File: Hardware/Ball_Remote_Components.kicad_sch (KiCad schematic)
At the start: 51 parts, among them J1 USB_B_Micro, J2 I2C_Gyro_Module, J3 SWD_Header, Q1 SI2333DS, U1 STM32WB35, U2 L3GD20, U3 MCP73831-2-OT, U4 LD3985M28R_SOT23, Y1 32MHz, Y2 32.768MHz

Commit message: Remote schematic and PCB clean up
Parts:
- added H1, H2: MountingHole, MountingHole:MountingHole_3.2mm_M3, symbol Mechanical:MountingHole
- added R2: 100k, Resistor_SMD:R_0603_1608Metric, symbol Device:R_Small
- added SW1: SW_SPDT, Custom_Footprints:SPDT_Slide_Switch, symbol Switch:SW_SPDT
- J1: renamed from J2; footprint Connector_PinSocket_2.54mm:PinSocket_1x06_P2.54mm_Vertical -> Connector_PinSocket_2.54mm:PinSocket_1x10_P2.54mm_Vertical; symbol Connector:Conn_01x06_Male -> Connector:Conn_01x10_Male
- renumbered C7 to C10, C18 to C11, C19 to C12, C14 to C13, C8 to C14, C9 to C15, C12 to C16, C13 to C17, C20 to C18, C21 to C19, C10 to C2, C22 to C20, C15 to C21, C16 to C22, C11 to C3, C17 to C4, C2 to C5, C3 to C6, C4 to C7, C5 to C8, C6 to C9, D2 to D1, D3 to D2, D1 to D3, J1 to J2, R3 to R1, R6 to R3, R2 to R4, R4 to R5, R5 to R6, R1 to R8, U3 to U1, U1 to U3
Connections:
- net +3V3 is gone; now on net +2V8: J3.1 (Pin_1)
- net GND: now also R2.1
- net USB_VIN: now also R2.2
- net BATT_+ renamed BATT_ON_OFF
- net BATT_ON_OFF: now also SW1.1 (A); no longer BT1.1 (+)
- new net BATT+: BT1.1 (+), SW1.2 (B)
- no-connect marks 16 -> 21
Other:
- note added: "Gyroscope and USB"
- note added: "LED/Buttons"
- note added: "MCU and RF"
- note added: "VCC will be 5V when connected to USB or 3.7-4.3V when battery powered NB R2 is pull-down for Q1"
- note removed: "Connectors/Buttons"
- note removed: "MCU"
- note removed: "VCC will be 5V when connected to USB or 3.7-4.3V when battery powered"
- moved on the sheet: AE1, C11, C12, C13, C18, C19, C2, C20, C21, C22, C3, C4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

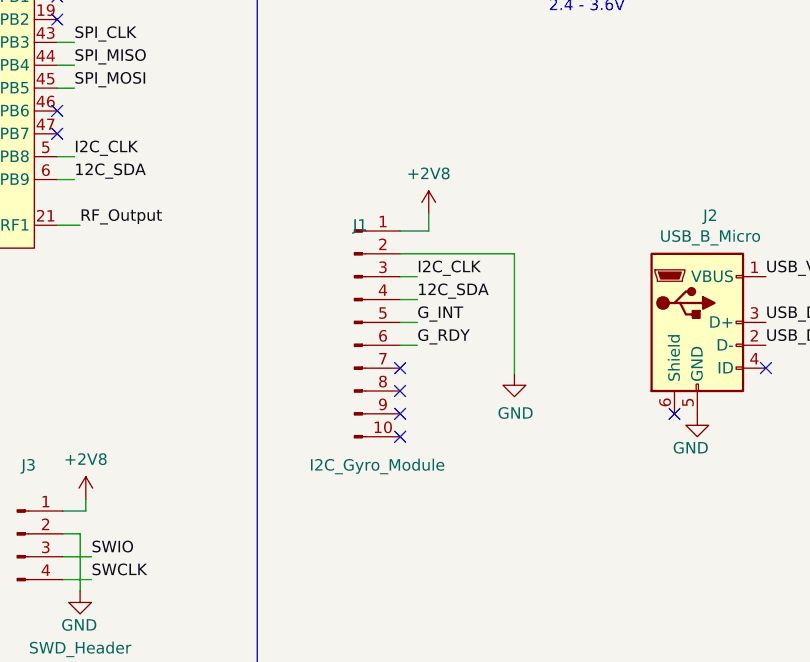
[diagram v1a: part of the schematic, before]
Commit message: More PCB clean-up
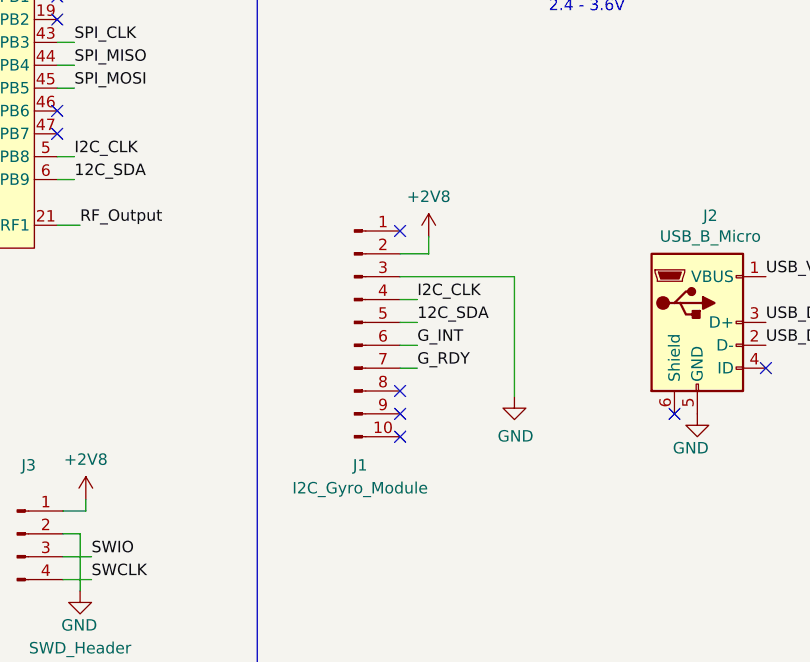
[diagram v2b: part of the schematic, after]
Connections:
- net +2V8: now also J1.2 (Pin_2); no longer J1.1 (Pin_1)
- net 12C_SDA: now also J1.5 (Pin_5); no longer J1.4 (Pin_4)
- net GND: now also J1.3 (Pin_3); no longer J1.2 (Pin_2)
- net G_INT: now also J1.6 (Pin_6); no longer J1.5 (Pin_5)
- net G_RDY: now also J1.7 (Pin_7); no longer J1.6 (Pin_6)
- net I2C_CLK: now also J1.4 (Pin_4); no longer J1.3 (Pin_3)
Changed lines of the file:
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@@
   (no_connect (at 86.995 77.47))
   (no_connect (at 86.995 92.71))
+  (no_connect (at 125.095 106.045))
   (no_connect (at 86.995 95.25))
   (no_connect (at 86.995 46.99))
@@
   (no_connect (at 56.515 95.25))
   (no_connect (at 125.095 126.365))
-  (no_connect (at 125.095 121.285))
   (wire (pts (xy 254.635 42.545) (xy 267.97 42.545))
     (stroke (width 0) (type default) (color 0 0 0 0))
@@
     (stroke (width 0) (type default) (color 0 0 0 0))
   )
-  (wire (pts (xy 125.095 106.045) (xy 128.27 106.045))
+  (wire (pts (xy 125.095 108.585) (xy 128.27 108.585))
     (stroke (width 0) (type default) (color 0 0 0 0))
   )
@@
     (stroke (width 0) (type default) (color 0 0 0 0))
   )
-  (wire (pts (xy 125.095 116.205) (xy 127 116.205))
-    (stroke (width 0) (type default) (color 0 0 0 0))
-  )
   (wire (pts (xy 125.095 118.745) (xy 127 118.745))
     (stroke (width 0) (type default) (color 0 0 0 0))
   )
+  (wire (pts (xy 125.095 121.285) (xy 127 121.285))
+    (stroke (width 0) (type default) (color 0 0 0 0))
+  )
   (wire (pts (xy 199.39 33.02) (xy 212.09 33.02))
     (stroke (width 0) (type default) (color 0 0 0 0))
@@
     (stroke (width 0) (type default) (color 0 0 0 0))
   )
-  (wire (pts (xy 137.795 108.585) (xy 137.795 121.92))
+  (wire (pts (xy 137.795 111.125) (xy 137.795 124.46))
     (stroke (width 0) (type default) (color 0 0 0 0))
   )
@@
     (stroke (width 0) (type default) (color 0 0 0 0))
   )
-  (wire (pts (xy 125.095 108.585) (xy 137.795 108.585))
+  (wire (pts (xy 125.095 111.125) (xy 137.795 111.125))
     (stroke (width 0) (type default) (color 0 0 0 0))
   )
@@
     (stroke (width 0) (type default) (color 0 0 0 0))
   )
-  (wire (pts (xy 128.27 106.045) (xy 128.27 104.14))
+  (wire (pts (xy 128.27 108.585) (xy 128.27 106.68))
     (stroke (width 0) (type default) (color 0 0 0 0))
   )
@@
     (stroke (width 0) (type default) (color 0 0 0 0))
   )
+  (wire (pts (xy 125.095 116.205) (xy 127 116.205))
+    (stroke (width 0) (type default) (color 0 0 0 0))
+  )
+  (wire (pts (xy 86.995 64.77) (xy 88.9 64.77))
+    (stroke (width 0) (type default) (color 0 0 0 0))
+  )
+  (wire (pts (xy 199.39 48.895) (xy 199.39 47.625))
+    (stroke (width 0) (type default) (color 0 0 0 0))
+  )
+  (wire (pts (xy 53.975 102.87) (xy 56.515 102.87))
+    (stroke (width 0) (type default) (color 0 0 0 0))
+  )
+  (wire (pts (xy 162.56 31.115) (xy 162.56 32.385))
+    (stroke (width 0) (type default) (color 0 0 0 0))
+  )
+  (wire (pts (xy 46.355 24.13) (xy 46.355 25.4))
+    (stroke (width 0) (type default) (color 0 0 0 0))
+  )
+  (wire (pts (xy 125.73 63.5) (xy 128.905 63.5))
+    (stroke (width 0) (type default) (color 0 0 0 0))
+  )
+  (wire (pts (xy 16.51 41.91) (xy 23.495 41.91))
+    (stroke (width 0) (type default) (color 0 0 0 0))
+  )
+  (wire (pts (xy 39.37 145.415) (xy 44.45 145.415))
+    (stroke (width 0) (type default) (color 0 0 0 0))
+  )
+  (wire (pts (xy 220.98 130.175) (xy 229.235 130.175))
+    (stroke (width 0) (type default) (color 0 0 0 0))
+  )
+  (wire (pts (xy 128.905 66.04) (xy 125.73 66.04))
+    (stroke (width 0) (type default) (color 0 0 0 0))
+  )
+  (wire (pts (xy 222.25 47.625) (xy 224.155 47.625))
+    (stroke (width 0) (type default) (color 0 0 0 0))
+  )
   (wire (pts (xy 125.095 113.665) (xy 127 113.665))
-    (stroke (width 0) (type default) (color 0 0 0 0))
-  )
-  (wire (pts (xy 86.995 64.77) (xy 88.9 64.77))
-    (stroke (width 0) (type default) (color 0 0 0 0))
-  )
-  (wire (pts (xy 199.39 48.895) (xy 199.39 47.625))
-    (stroke (width 0) (type default) (color 0 0 0 0))
-  )
-  (wire (pts (xy 53.975 102.87) (xy 56.515 102.87))
-    (stroke (width 0) (type default) (color 0 0 0 0))
-  )
-  (wire (pts (xy 162.56 31.115) (xy 162.56 32.385))
-    (stroke (width 0) (type default) (color 0 0 0 0))
-  )
-  (wire (pts (xy 46.355 24.13) (xy 46.355 25.4))
-    (stroke (width 0) (type default) (color 0 0 0 0))
-  )
-  (wire (pts (xy 125.73 63.5) (xy 128.905 63.5))
-    (stroke (width 0) (type default) (color 0 0 0 0))
-  )
-  (wire (pts (xy 16.51 41.91) (xy 23.495 41.91))
-    (stroke (width 0) (type default) (color 0 0 0 0))
-  )
-  (wire (pts (xy 39.37 145.415) (xy 44.45 145.415))
-    (stroke (width 0) (type default) (color 0 0 0 0))
-  )
-  (wire (pts (xy 220.98 130.175) (xy 229.235 130.175))
-    (stroke (width 0) (type default) (color 0 0 0 0))
-  )
-  (wire (pts (xy 128.905 66.04) (xy 125.73 66.04))
-    (stroke (width 0) (type default) (color 0 0 0 0))
-  )
-  (wire (pts (xy 222.25 47.625) (xy 224.155 47.625))
-    (stroke (width 0) (type default) (color 0 0 0 0))
-  )
-  (wire (pts (xy 125.095 111.125) (xy 127 111.125))
     (stroke (width 0) (type default) (color 0 0 0 0))
   )
@@
     (effects (font (size 1.27 1.27)) (justify right bottom))
   )
-  (label "G_INT" (at 127 116.205 0)
+  (label "G_INT" (at 127 118.745 0)
     (effects (font (size 1.27 1.27)) (justify left bottom))
   )
@@
     (effects (font (size 1.27 1.27)) (justify left bottom))
   )
-  (label "I2C_CLK" (at 127 111.125 0)
+  (label "I2C_CLK" (at 127 113.665 0)
     (effects (font (size 1.27 1.27)) (justify left bottom))
   )
@@
     (effects (font (size 1.27 1.27)) (justify left bottom))
   )
-  (label "12C_SDA" (at 127 113.665 0)
+  (label "12C_SDA" (at 127 116.205 0)
     (effects (font (size 1.27 1.27)) (justify left bottom))
   )
@@
     (effects (font (size 1.27 1.27)) (justify left bottom))
   )
-  (label "G_RDY" (at 127 118.745 0)
+  (label "G_RDY" (at 127 121.285 0)
     (effects (font (size 1.27 1.27)) (justify left bottom))
   )
@@
   )
   (symbol (lib_id "Connector:Conn_01x10_Male") (at 120.015 116.205 0) (unit 1)
-    (in_bom yes) (on_board yes)
-    (property "Reference" "J1" (id 0) (at 120.65 105.41 0))
-    (property "Value" "I2C_Gyro_Module" (id 1) (at 122.555 132.08 0))
+    (in_bom yes) (on_board yes) (fields_autoplaced)
+    (property "Reference" "J1" (id 0) (at 120.65 132.08 0))
+    (property "Value" "I2C_Gyro_Module" (id 1) (at 120.65 134.62 0))
     (property "Footprint" "Connector_PinSocket_2.54mm:PinSocket_1x10_P2.54mm_Vertical" (id 2) (at 120.015 116.205 0)
       (effects (font (size 1.27 1.27)) hide)
@@
     (pin "1")
   )
-  (symbol (lib_id "power:+2V8") (at 128.27 104.14 0) (unit 1)
-    (in_bom yes) (on_board yes)
-    (property "Reference" "#PWR026" (id 0) (at 128.27 107.95 0)
-      (effects (font (size 1.27 1.27)) hide)
-    )
-    (property "Value" "+2V8" (id 1) (at 128.27 99.695 0))
-    (property "Footprint" "" (id 2) (at 128.27 104.14 0)
-      (effects (font (size 1.27 1.27)) hide)
-    )
-    (property "Datasheet" "" (id 3) (at 128.27 104.14 0)
+  (symbol (lib_id "power:+2V8") (at 128.27 106.68 0) (unit 1)
+    (in_bom yes) (on_board yes)
+    (property "Reference" "#PWR026" (id 0) (at 128.27 110.49 0)
+      (effects (font (size 1.27 1.27)) hide)
+    )
+    (property "Value" "+2V8" (id 1) (at 128.27 102.235 0))
+    (property "Footprint" "" (id 2) (at 128.27 106.68 0)
+      (effects (font (size 1.27 1.27)) hide)
+    )
+    (property "Datasheet" "" (id 3) (at 128.27 106.68 0)
       (effects (font (size 1.27 1.27)) hide)
     )
@@
     (pin "2")
   )
-  (symbol (lib_id "power:GND") (at 137.795 121.92 0) (unit 1)
-    (in_bom yes) (on_board yes)
-    (property "Reference" "#PWR031" (id 0) (at 137.795 128.27 0)
-      (effects (font (size 1.27 1.27)) hide)
-    )
-    (property "Value" "GND" (id 1) (at 137.922 126.3142 0))
-    (property "Footprint" "" (id 2) (at 137.795 121.92 0)
-      (effects (font (size 1.27 1.27)) hide)
-    )
-    (property "Datasheet" "" (id 3) (at 137.795 121.92 0)
-      (effects (font (size 1.27 1.27)) hide)
-    )
+  (symbol (lib_id "power:GND") (at 137.795 124.46 0) (unit 1)
+    (in_bom yes) (on_board yes)
+    (property "Reference" "#PWR031" (id 0) (at 137.795 130.81 0)
+      (effects (font (size 1.27 1.27)) hide)
+    )
+    (property "Value" "GND" (id 1) (at 137.922 128.8542 0))
+    (property "Footprint" "" (id 2) (at 137.795 124.46 0)
+      (effects (font (size 1.27 1.27)) hide)
+    )
+    (property "Datasheet" "" (id 3) (at 137.795 124.46 0)
+      (effects (font (size 1.27 1.27)) hide)
+    )

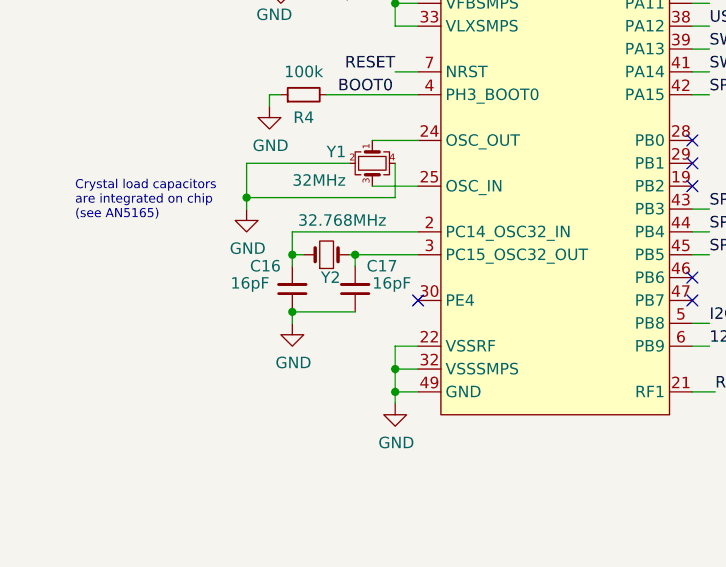
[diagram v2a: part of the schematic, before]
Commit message: Created test firmware for STM32WB35 hardware (not yet working)
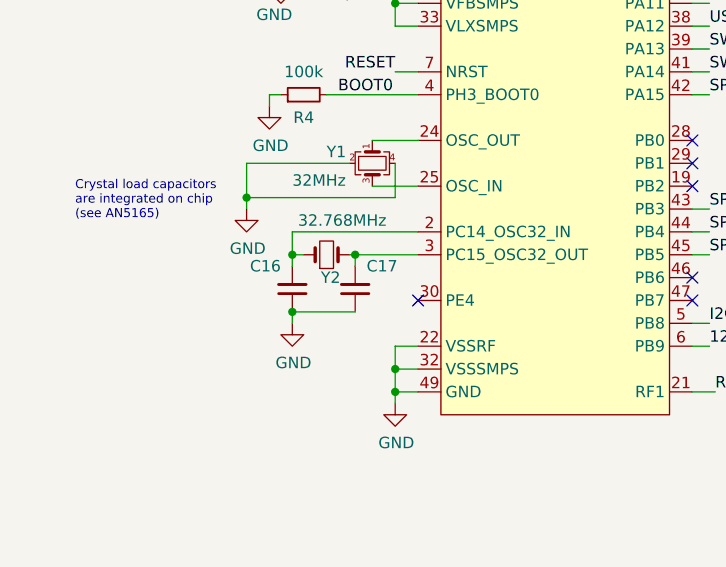
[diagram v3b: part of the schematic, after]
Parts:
- C16, C17: value 16pF -> (none)
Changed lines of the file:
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@@
       (effects (font (size 1.27 1.27)) (justify left))
     )
-    (property "Value" "16pF" (id 1) (at 40.005 93.345 0)
+    (property "Value" "" (id 1) (at 40.005 93.345 0)
       (effects (font (size 1.27 1.27)) (justify left))
     )
@@
       (effects (font (size 1.27 1.27)) (justify right))
     )
-    (property "Value" "16pF" (id 1) (at 51.435 93.345 0)
+    (property "Value" "" (id 1) (at 51.435 93.345 0)
       (effects (font (size 1.27 1.27)) (justify right))
     )
@@
     )
     (path "/590a4ace-48fb-4f4a-888d-cb64d1d49ec8"
-      (reference "C16") (unit 1) (value "16pF") (footprint "Capacitor_SMD:C_0603_1608Metric")
+      (reference "C16") (unit 1) (value "20pF") (footprint "Capacitor_SMD:C_0603_1608Metric")
     )
     (path "/c5015d8e-772d-4539-bdc3-01884b4e5a2c"
-      (reference "C17") (unit 1) (value "16pF") (footprint "Capacitor_SMD:C_0603_1608Metric")
+      (reference "C17") (unit 1) (value "20pF") (footprint "Capacitor_SMD:C_0603_1608Metric")
     )
     (path "/d86a617d-114d-4fd7-a3c8-43b5be3b3585"

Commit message: Preparing to test Remote board
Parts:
- C16, C17: value (none) -> 20pF

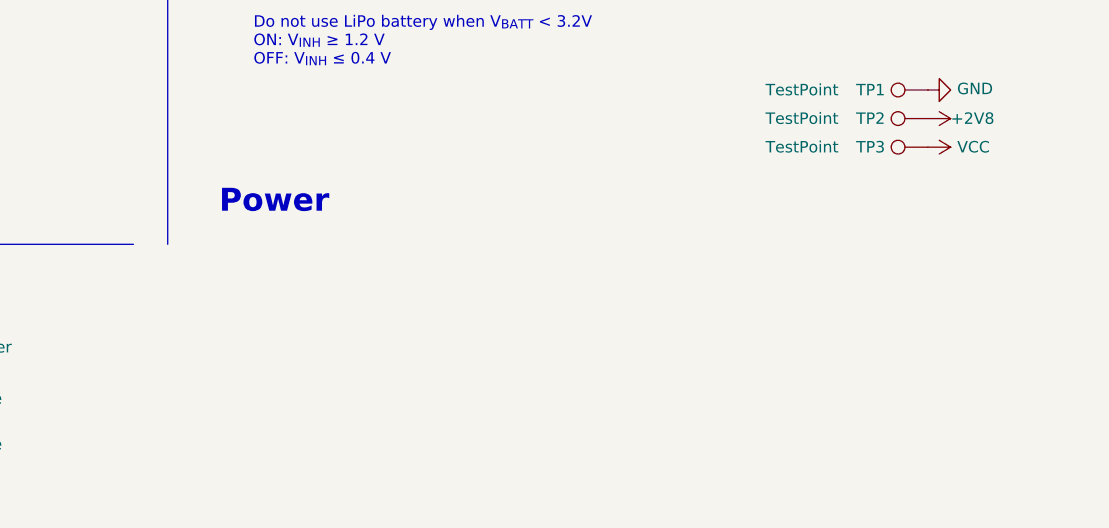
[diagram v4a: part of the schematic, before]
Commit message: Updating Gyroscope code to use SPI
Basic communication with Gyro SPI working; DMA not yet implemented
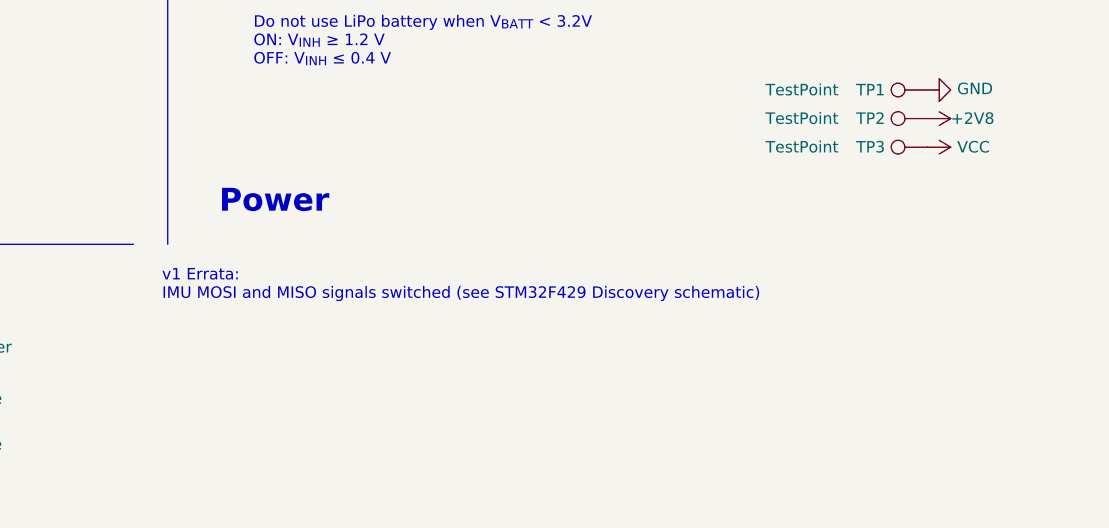
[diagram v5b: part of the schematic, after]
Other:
- note added: "v1 Errata: IMU MOSI and MISO signals switched (see STM32F429 Discovery schematic)"
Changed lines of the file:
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@@
+    (effects (font (size 1.27 1.27)) (justify left bottom))
+  )
+  (text "v1 Errata:\nIMU MOSI and MISO signals switched (see STM32F429 Discovery schematic)"
+    (at 180.34 172.72 0)
     (effects (font (size 1.27 1.27)) (justify left bottom))
   )

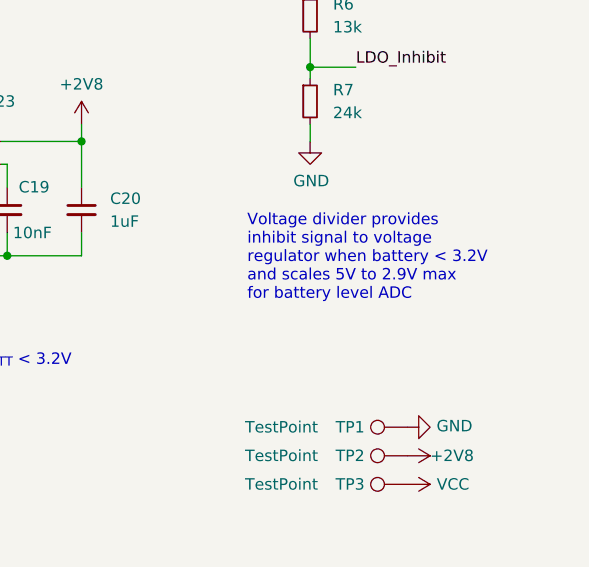
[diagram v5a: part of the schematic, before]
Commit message: Added Battery Voltage output to BAS service
Fixed RSSI output
Fixed bug sequencing gyro SPI reads
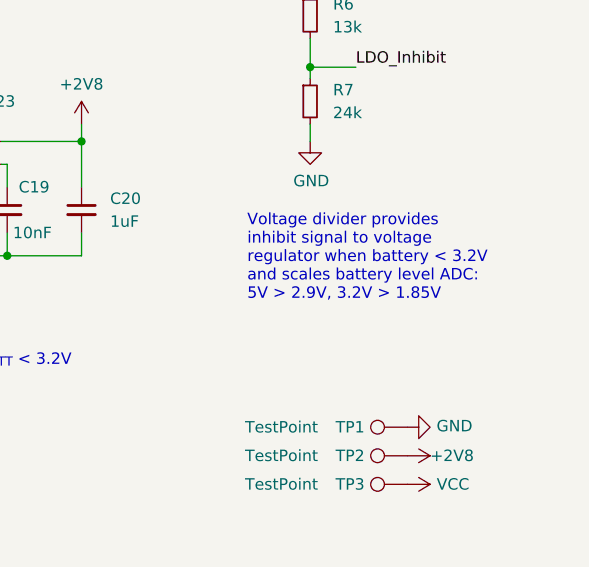
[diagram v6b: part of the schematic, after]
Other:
- note added: "Voltage divider provides inhibit signal to voltage regulator when battery < 3.2V and scales battery level ADC: 5V > 2.9V, 3.2V > 1.85V"
- note removed: "Voltage divider provides inhibit signal to voltage regulator when battery < 3.2V and scales 5V to 2.9V max for battery level ADC"
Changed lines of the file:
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@@
     (effects (font (size 1.27 1.27)) (justify left bottom))
   )
-  (text "Voltage divider provides\ninhibit signal to voltage \nregulator when battery < 3.2V \nand scales 5V to 2.9V max \nfor battery level ADC"
+  (text "Voltage divider provides\ninhibit signal to voltage \nregulator when battery < 3.2V \nand scales battery level ADC:\n5V > 2.9V, 3.2V > 1.85V"
     (at 247.65 135.255 0)
     (effects (font (size 1.27 1.27)) (justify left bottom))
